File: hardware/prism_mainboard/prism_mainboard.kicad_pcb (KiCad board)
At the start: 6 copper layers, 100 x 100 mm, 82 parts, among them IC1 KTDM4G3C618BGIEAT, IC2 KTDM4G3C618BGIEAT, IC3 USB3320C-EZK, J1 503398-1892, J2 UJ32-21-C-H-G-HMT-LT-P24-TR, U1 XC7Z015-2CLG485I, U2 LMS7002M, U3 PEC16-4220F-S0024, U4 AMS1117-1.8, U5 AMS1117-1.8, U6 AMS1117-1.8, U7 AMS1117-1.8

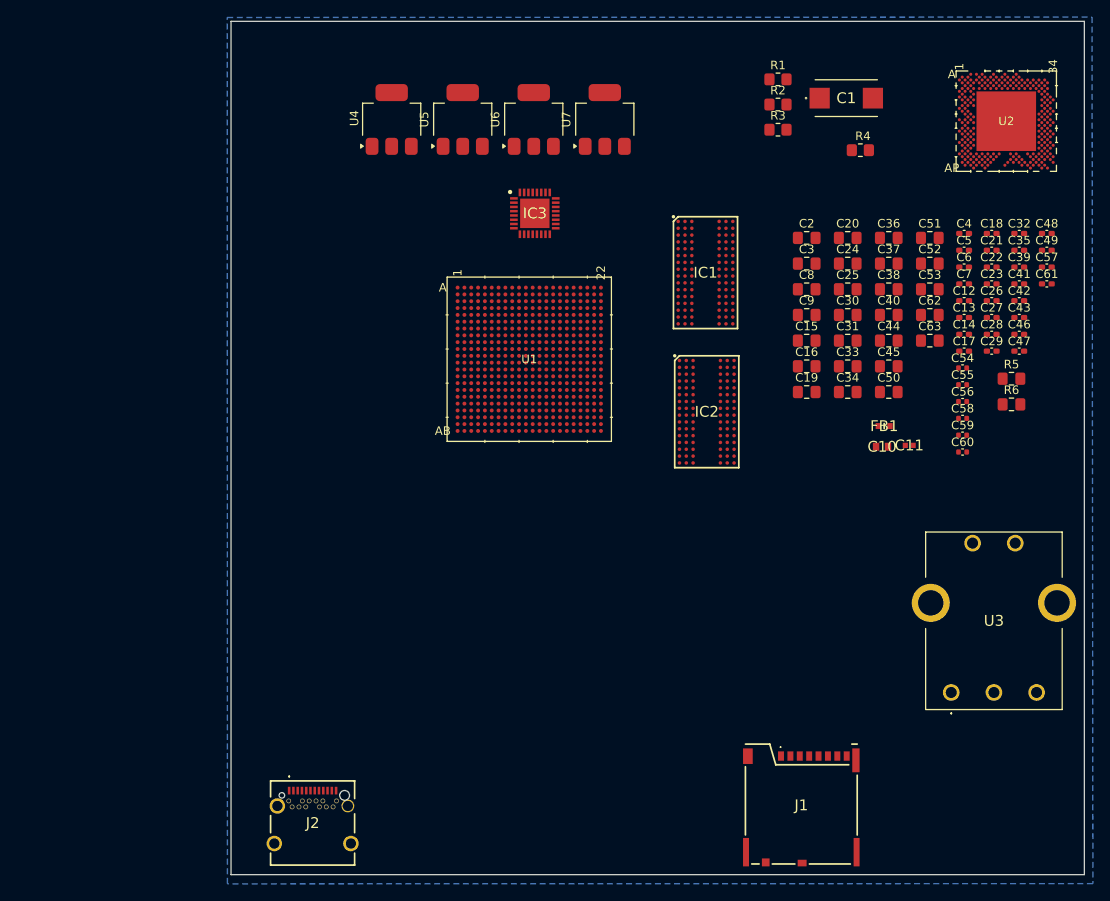
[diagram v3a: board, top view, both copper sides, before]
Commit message: Layout Updates
Started organizing some of the components on the PCB layout. Have not started routing yet but intend on doing the simple / slow traces first.
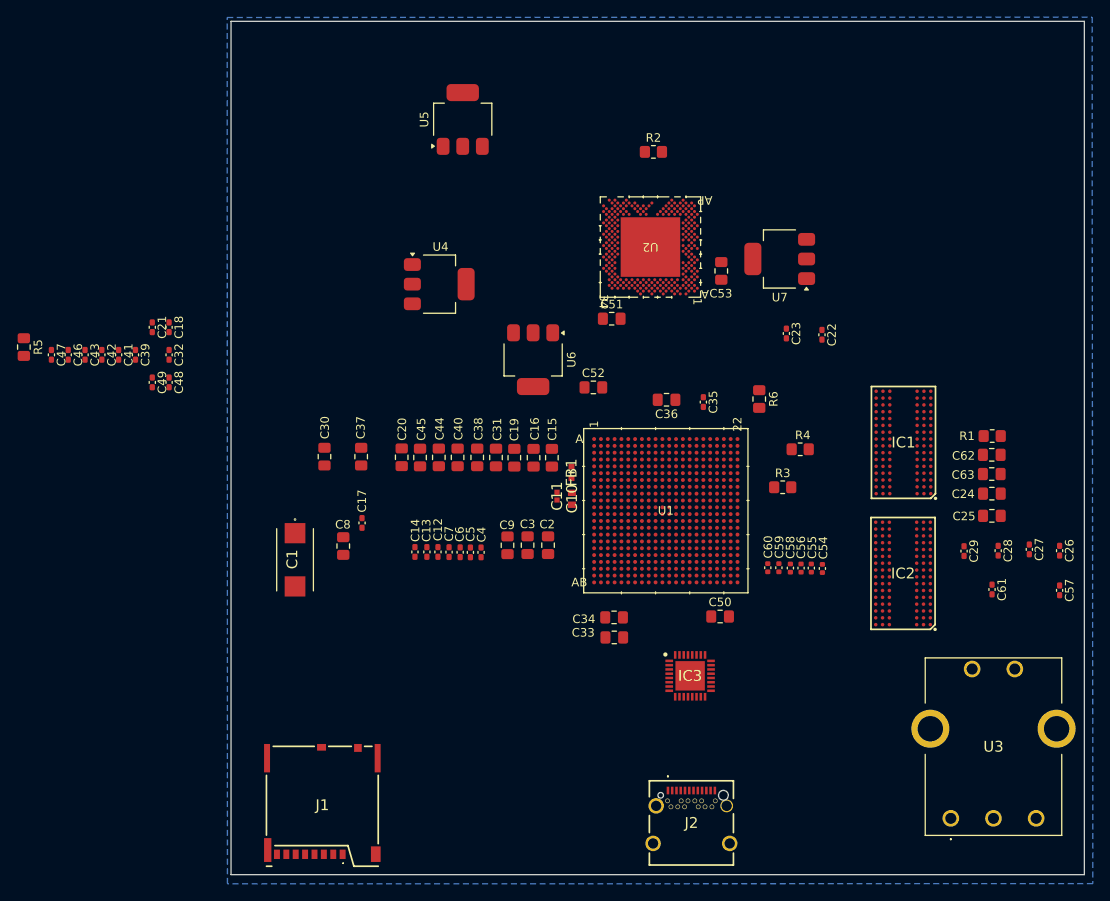
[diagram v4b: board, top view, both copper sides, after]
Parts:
- moved R5 115.8 mm to (53.4, 95.0), turned to -90 degrees
- moved C47 113.4 mm to (56.6, 95.9), turned to -90 degrees
- moved C46 111.5 mm to (58.6, 95.9), turned to -90 degrees
- moved C43 109.6 mm to (60.5, 95.9), turned to -90 degrees
- moved C42 107.7 mm to (62.5, 95.9), turned to -90 degrees
- moved C49 106.0 mm to (68.4, 99.1), turned to -90 degrees
- moved C41 105.9 mm to (64.5, 95.9), turned to -90 degrees
- moved C48 104.3 mm to (70.4, 99.1), turned to -90 degrees
- moved C39 104.1 mm to (66.5, 95.9), turned to -90 degrees
- moved C32 100.6 mm to (70.4, 95.9), turned to -90 degrees
- moved C21 98.8 mm to (68.4, 92.7), turned to -90 degrees
- moved C18 97.0 mm to (70.4, 92.7), turned to -90 degrees
- moved C1 84.3 mm to (85.2, 119.9), turned to -90 degrees
- moved C17 73.4 mm to (93.0, 115.6), turned to -90 degrees
- moved C14 69.2 mm to (99.2, 119.0), turned to -90 degrees
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
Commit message: Layout Update and References
Small layout updates, and added some SDR references to see what I can take from them.
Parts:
- moved C49 47.7 mm to (115.5, 106.9), turned to 90 degrees
- moved C48 44.8 mm to (114.5, 106.9), turned to 90 degrees
- moved C17 22.3 mm to (113.5, 106.9), turned to 90 degrees
- moved C15 3.75 mm to (111.5, 107.9)
- moved C16 3.75 mm to (109.3, 107.9)
- moved C19 3.75 mm to (107.1, 107.9)
- moved C20 3.75 mm to (93.9, 107.9)
- moved C31 3.75 mm to (105.0, 107.9)
- moved C38 3.75 mm to (102.8, 107.9)
- moved C40 3.75 mm to (100.5, 107.9)
- moved C44 3.75 mm to (98.2, 107.9)
- moved C45 3.75 mm to (96.0, 107.9)
- moved C37 1.40 mm to (91.5, 107.8)
- moved C30 1.00 mm to (87.6, 107.8)
- moved FB1 0.35 mm to (117.5, 109.3)

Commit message: Autosave bug update
Sometimes autosave bugs and saves the same thing but at a future time. This is just to consolidate and keep github up to date. No changes have been made
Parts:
- moved C50 35.5 mm to (128.6, 91.6)
- moved C42 30.5 mm to (93.0, 97.9)
- moved C43 30.5 mm to (91.0, 97.9)
- moved C46 30.5 mm to (89.0, 97.9)
- moved C47 30.5 mm to (87.1, 97.9)
- moved R5 30.5 mm to (83.8, 97.0)
- moved C18 30.5 mm to (100.8, 94.7)
- moved C21 30.5 mm to (98.9, 94.7)
- moved C32 30.5 mm to (100.8, 97.9)
- moved C39 30.5 mm to (96.9, 97.9)
- moved C41 30.5 mm to (94.9, 97.9)
- moved C17 22.3 mm to (93.0, 115.6), turned to -90 degrees
- moved C49 17.6 mm to (98.9, 101.1), turned to -90 degrees
- moved C48 14.8 mm to (100.8, 101.1), turned to -90 degrees
- moved C15 3.75 mm to (115.2, 107.9)
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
